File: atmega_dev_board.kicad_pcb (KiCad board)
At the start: 2 copper layers, 40 parts, among them J1 GPIO Header, J2 USB_B_Micro, J3 GPIO Header, J4 ICSP Header, Q1 Q_PMOS_DGS, SW1 SW_Push, U1 LM358, U2 NCV8114ASN330T1G, U3 NCV8114ASN330T1G, U4 ATmega328P-A, U5 CH340G, Y1 Crystal_GND23, Y2 Crystal_GND23

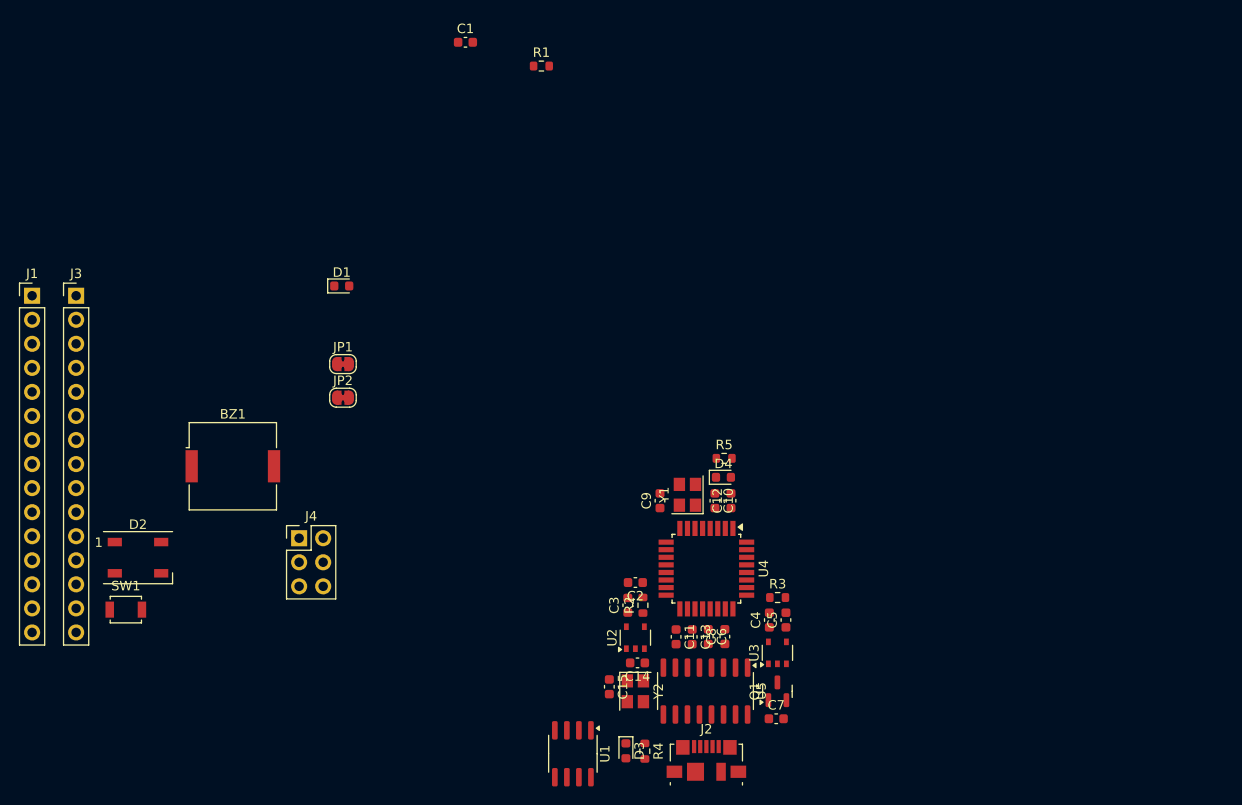
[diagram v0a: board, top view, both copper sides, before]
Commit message: Move to USB C and CP2102
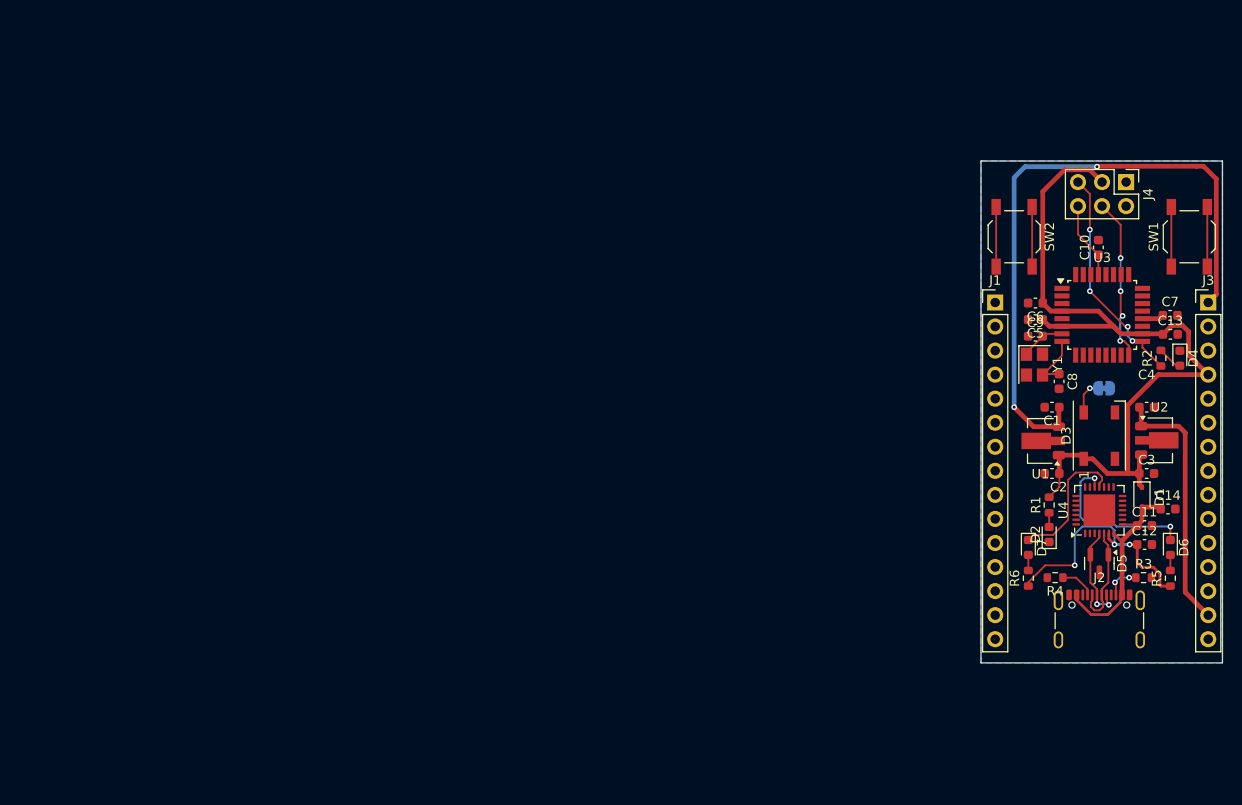
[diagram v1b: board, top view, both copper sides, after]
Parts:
- removed BZ1: Buzzer, Buzzer_Beeper:Buzzer_Murata_PKMCS0909E
- removed C15: 22p, Capacitor_SMD:C_0603_1608Metric
- removed JP2: Solder Jumper NC, Jumper:SolderJumper-2_P1.3mm_Bridged_RoundedPad1.0x1.5mm
- removed Q1: Q_PMOS_DGS, Package_TO_SOT_SMD:SOT-23
- removed U5: CH340G, Package_SO:SOIC-16_3.9x9.9mm_P1.27mm
- removed Y2: Crystal_GND23, Crystal:Crystal_SMD_3225-4Pin_3.2x2.5mm
- added D5: SM712_SOT23, Package_TO_SOT_SMD:SOT-23, F.Cu at (228.5, 117.0)
- added D6: LED, LED_SMD:LED_0603_1608Metric, F.Cu at (236.0, 115.3)
- added D7: LED, LED_SMD:LED_0603_1608Metric, F.Cu at (221.0, 115.3)
- added R6: 1k, Resistor_SMD:R_0603_1608Metric, F.Cu at (221.0, 118.6)
- added SW2: Push button switch, Button_Switch_SMD:SW_SPST_TL3342, F.Cu at (219.5, 82.5)
- C10: value 22p -> 100n
- C11, C2, C4, C5: value 10u -> 100n
- C14: value 22p -> 10u
- C8: value 100n -> 22p
- D1: value D_Small -> Diode Schottky; footprint Diode_SMD:D_0603_1608Metric -> Diode_SMD:D_SOD-323
- D2: value WS2812B -> LED; footprint LED_SMD:LED_WS2812B_PLCC4_5.0x5.0mm_P3.2mm -> LED_SMD:LED_0603_1608Metric
- D3: value LED_Small -> WS2812B; footprint LED_SMD:LED_0603_1608Metric -> LED_SMD:LED_WS2812B_PLCC4_5.0x5.0mm_P3.2mm
- D4: value LED_Small -> LED
- J1, J3: value GPIO Header -> 1x15 Pin Header
- J2: value USB_B_Micro -> USB_C_Receptacle_USB2.0_16P; footprint Connector_USB:USB_Micro-B_Molex_47346-0001 -> Connector_USB:USB_C_Receptacle_GCT_USB4105-xx-A_16P_TopMnt_Horizontal
- JP1: value Solder Jumper NC -> Closed Solder Jumper; moved to B.Cu
- R1: value 100 -> 1k
- R3, R4: value 1k -> 5k1
- SW1: value SW_Push -> Push button switch; footprint Button_Switch_SMD:SW_SPST_B3U-1000P -> Button_Switch_SMD:SW_SPST_TL3342
- U1: value LM358 -> L78L05_SOT89; footprint Package_SO:SOIC-8_3.9x4.9mm_P1.27mm -> Package_TO_SOT_SMD:SOT-89-3
- U2: value NCV8114ASN330T1G -> L78L33_SOT89; footprint Package_SO:TSOP-5_1.65x3.05mm_P0.95mm -> Package_TO_SOT_SMD:SOT-89-3
- U3: value NCV8114ASN330T1G -> ATmega328P-A; footprint Package_SO:TSOP-5_1.65x3.05mm_P0.95mm -> Package_QFP:TQFP-32_7x7mm_P0.8mm
- U4: value ATmega328P-A -> CP2102N-Axx-xQFN28; footprint Package_QFP:TQFP-32_7x7mm_P0.8mm -> Package_DFN_QFN:QFN-28-1EP_5x5mm_P0.5mm_EP3.35x3.35mm
- Y1: value Crystal_GND23 -> Crystal 16MHz
- moved J3 119.6 mm to (240.0, 89.4)
- moved SW1 119.0 mm to (238.0, 82.5), turned to 90 degrees
- moved J1 101.7 mm to (217.5, 89.4)
- moved D2 96.3 mm to (223.2, 113.9), turned to 90 degrees
- moved J4 95.1 mm to (231.3, 76.7), turned to -90 degrees
- moved D1 87.4 mm to (233.0, 110.0), turned to -90 degrees
- moved JP1 80.4 mm to (229.0, 98.5), turned to 180 degrees
- moved C1 73.0 mm to (223.5, 100.5), turned to 180 degrees
- moved R1 70.9 mm to (223.2, 110.8), turned to -90 degrees
- moved R2 60.6 mm to (235.0, 95.3)
- moved D3 60.1 mm to (228.5, 103.5), turned to 90 degrees
- moved C13 59.8 mm to (236.0, 92.8), turned to 0 degrees
- moved C7 59.5 mm to (236.0, 90.8)
- moved U1 59.4 mm to (222.3, 104.1), turned to 180 degrees
- moved U2 59.2 mm to (234.9, 104.0), turned to 0 degrees
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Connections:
- C1 pad 1: +5V -> +VDC
- C10 pad 1: GND -> /RESET
- C10 pad 2: Net-(U4-XTAL1/PB6) -> GND
- C11 pad 1: +5V -> VBUS
- C12 pad 1: +5V -> /CP_VDD
- C14 pad 1: /CH_XI -> VBUS
- C3 pad 1: +VDC -> +5V
- C4 pad 1: +5V -> +3V3
- C5 pad 1: +3V3 -> +5V
- C6 pad 1: /AREF -> +5V
- C7 pad 1: VBUS -> /AREF
- C8 pad 1: /CH_3V -> /AT_XTAL2
- C9 pad 1: Net-(U4-XTAL2/PB7) -> GND
- C9 pad 2: GND -> /AT_XTAL1
- D1 pad 1: /BZ+ -> +5V
- D1 pad 2: GND -> VBUS
- D2 pad 1: +5V -> GND
- D2 pad 2: unconnected-(D2-DOUT-Pad2) -> /LED_PWR
- D3 pad 1: GND -> +5V
- D3 pad 2: /LED_PWR -> unconnected-(D3-DOUT-Pad2)
- JP1 pad 1: /D9 -> /D11
- JP1 pad 2: /BZ+ -> /RGB_DIN
- R1 pad 1: /RGB_R -> +5V
- R1 pad 2: /RGB_DIN -> /LED_PWR
- R2 pad 1: +VDC -> /D13
- R2 pad 2: Net-(U2-EN) -> /LED_USR
- R3 pad 1: +5V -> /USB_CC2
- R3 pad 2: Net-(U3-EN) -> GND
- R4 pad 1: +5V -> /USB_CC1
- R4 pad 2: /LED_PWR -> GND
- R5 pad 1: /D13 -> /CP_VDD
- R5 pad 2: /LED_USR -> /LED_TXT
- SW1 pad 1: /RESET -> /D9
- U1 pad 1: Net-(Q1-G) -> +5V
- U1 pad 2: +3V3 -> GND
- U2 pad 1: +VDC -> +3V3
- U2 pad 3: Net-(U2-EN) -> +5V
- U3 pad 1: +5V -> /D3
- U3 pad 2: GND -> /D4
- U3 pad 3: Net-(U3-EN) -> GND
- U3 pad 4: unconnected-(U3-NC-Pad4) -> +5V
- U3 pad 5: +3V3 -> GND
- U4 pad 1: /D3 -> unconnected-(U4-~{DCD}-Pad1)
- U4 pad 10: /D6 -> unconnected-(U4-NC-Pad10)
- U4 pad 11: /D7 -> unconnected-(U4-~{SUSPEND}-Pad11)
- U4 pad 12: /D8 -> unconnected-(U4-SUSPEND-Pad12)
- U4 pad 13: /D9 -> unconnected-(U4-CHREN-Pad13)
- U4 pad 14: /D10 -> unconnected-(U4-CHR1-Pad14)
- U4 pad 15: /D11 -> unconnected-(U4-CHR0-Pad15)
- U4 pad 16: /D12 -> unconnected-(U4-~{WAKEUP}/GPIO.3-Pad16)
- U4 pad 17: /D13 -> unconnected-(U4-RS485/GPIO.2-Pad17)
- U4 pad 18: +5V -> /RXT
- U4 pad 19: /A6 -> /TXT
- U4 pad 2: /D4 -> unconnected-(U4-~{RI}/CLK-Pad2)
- U4 pad 20: /AREF -> unconnected-(U4-GPIO.6-Pad20)
- U4 pad 21: GND -> unconnected-(U4-GPIO.5-Pad21)
- U4 pad 22: /A7 -> unconnected-(U4-GPIO.4-Pad22)
- U4 pad 23: /A0 -> unconnected-(U4-~{CTS}-Pad23)
- U4 pad 24: /A1 -> unconnected-(U4-~{RTS}-Pad24)
- U4 pad 25: /A2 -> /D0
- U4 pad 26: /A3 -> /D1
- U4 pad 27: /A4 -> unconnected-(U4-~{DSR}-Pad27)
- U4 pad 28: /A5 -> /RESET
- U4 pad 29: /RESET -> GND
- U4 pad 4: +5V -> /USB_D+
- U4 pad 5: GND -> /USB_D-
- U4 pad 6: +5V -> /CP_VDD
- U4 pad 7: Net-(U4-XTAL1/PB6) -> VBUS
- U4 pad 8: Net-(U4-XTAL2/PB7) -> VBUS
- U4 pad 9: /D5 -> unconnected-(U4-~{RST}-Pad9)
- Y1 pad 1: Net-(U4-XTAL1/PB6) -> /AT_XTAL1
- Y1 pad 3: GND -> /AT_XTAL2
- Y1 pad 4: Net-(U4-XTAL2/PB7) -> GND
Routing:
- net +5V: track 0.00 -> 85.8 mm
- net +VDC: track 0.00 -> 67.7 mm, vias 0 -> 2
- net +3V3: track 0.00 -> 27.3 mm
- net /CP_VDD: track 0.00 -> 26.5 mm, vias 0 -> 3
- net /D13: track 0.00 -> 23.8 mm, vias 0 -> 4
- net VBUS: track 0.00 -> 23.5 mm
- net /TXT: track 0.00 -> 17.6 mm, vias 0 -> 2
- net /D12: track 0.00 -> 17.3 mm, vias 0 -> 4
- net /RXT: track 0.00 -> 14.6 mm
- net /RESET: track 0.00 -> 14.4 mm
- net GND: track 0.00 -> 12.6 mm
- net /USB_D-: track 0.00 -> 11.2 mm
- net /USB_D+: track 0.00 -> 10.6 mm, vias 0 -> 2
- net /D9: track 0.00 -> 6.30 mm
- net /AT_XTAL2: track 0.00 -> 6.19 mm
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- added copper zone on B.Cu, net GND
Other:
- board outline added: 25.5 x 53 mm

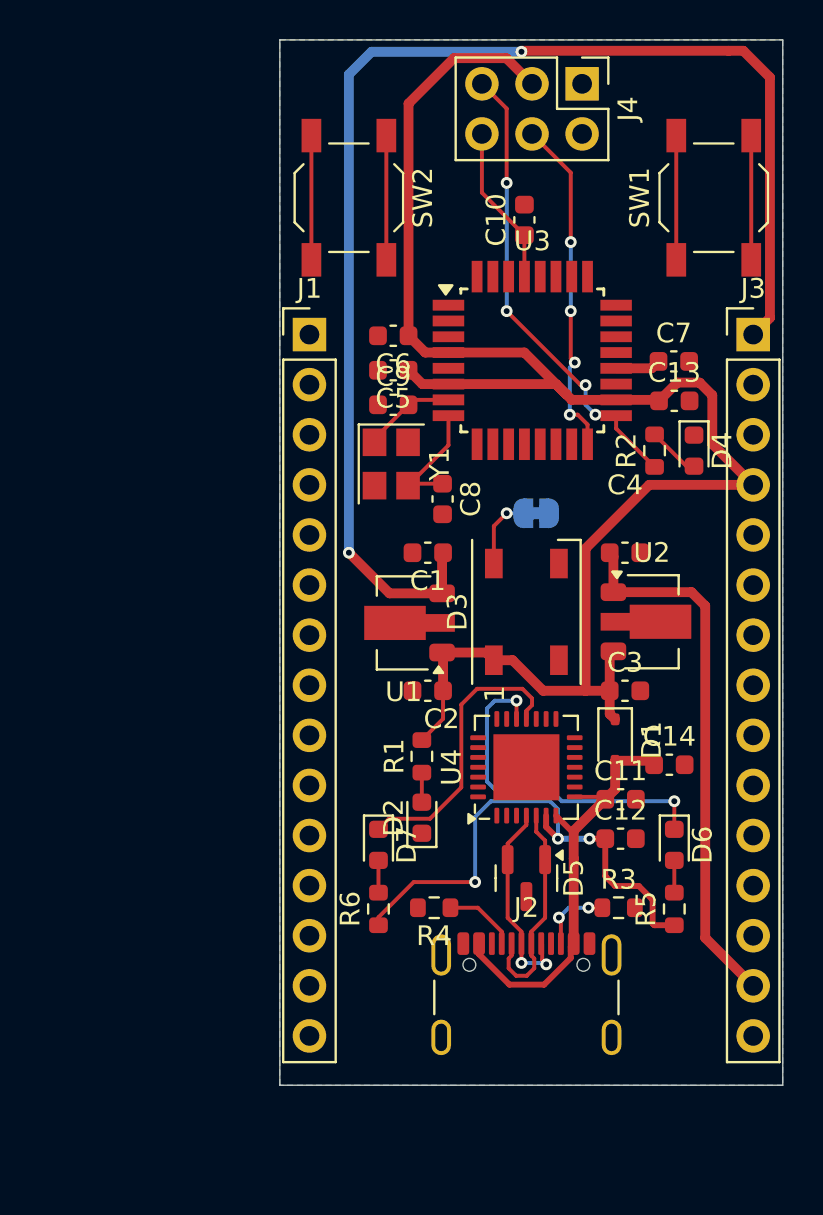
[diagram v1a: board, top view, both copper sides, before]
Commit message: Adjust pin header and board size to match 0m1" pitch
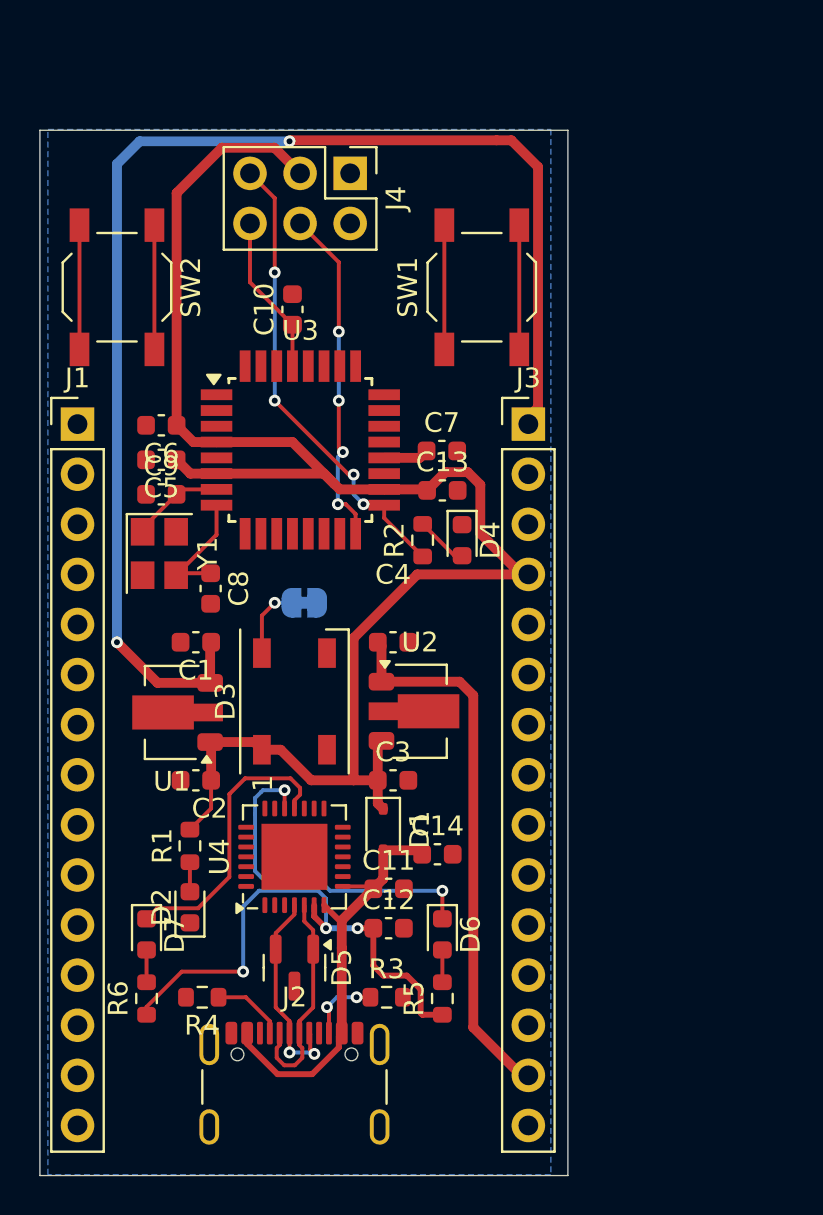
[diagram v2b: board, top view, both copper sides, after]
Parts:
- moved C10 12.6 mm to (216.6, 88.2)
- moved C11 12.6 mm to (221.5, 117.5)
- moved C12 12.6 mm to (221.5, 119.5)
- moved R3 12.6 mm to (221.4, 123.0)
- moved U2 12.6 mm to (223.1, 108.5)
- moved U3 12.6 mm to (217.0, 95.3)
- moved Y1 12.6 mm to (209.9, 100.5)
- moved U1 12.6 mm to (210.5, 108.6)
- moved C1 12.6 mm to (211.7, 105.0)
- moved C13 12.6 mm to (224.2, 97.3)
- moved C14 12.6 mm to (224.0, 115.8)
- moved C2 12.6 mm to (211.7, 112.0)
- moved C3 12.6 mm to (221.7, 112.0)
- moved C4 12.6 mm to (221.7, 105.0)
- moved C5 12.6 mm to (210.0, 95.8)
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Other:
- board size 25.5 x 53 mm -> 26.8 x 53 mm

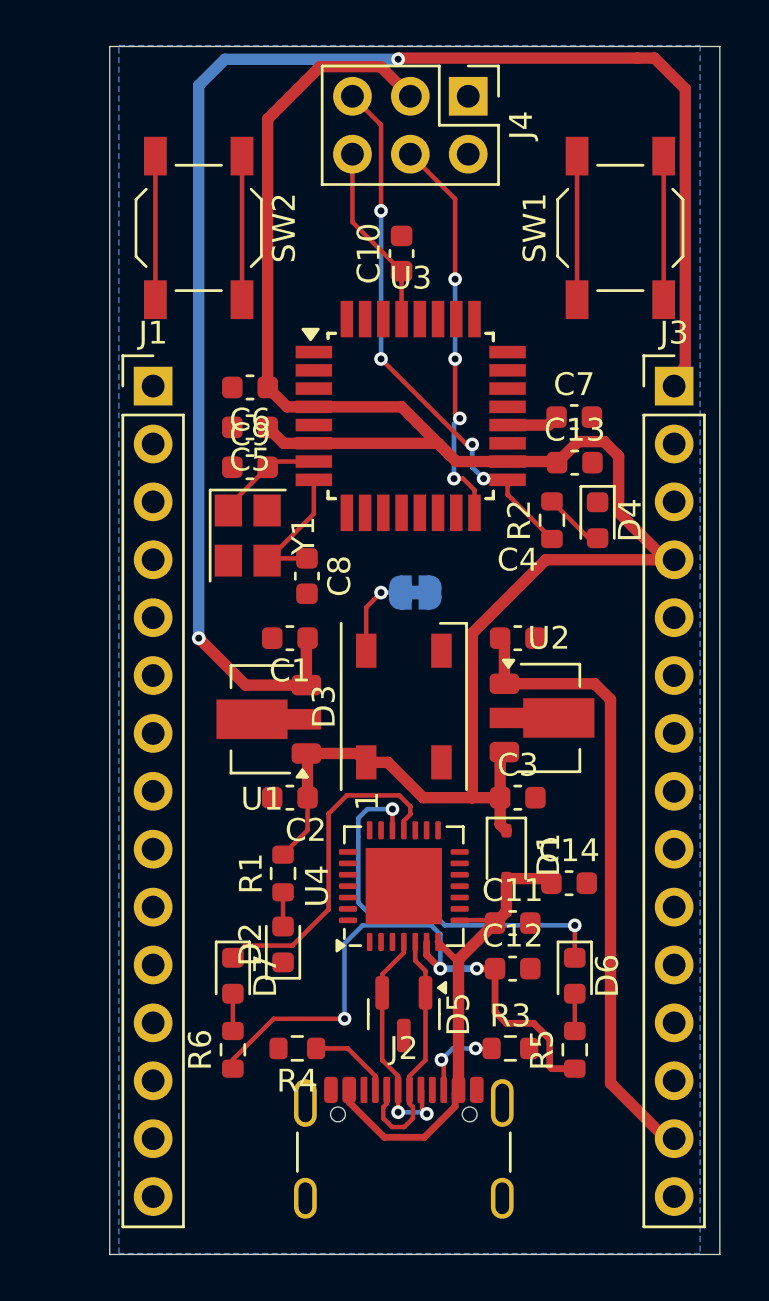
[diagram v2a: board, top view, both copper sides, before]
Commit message: New placements of PCB
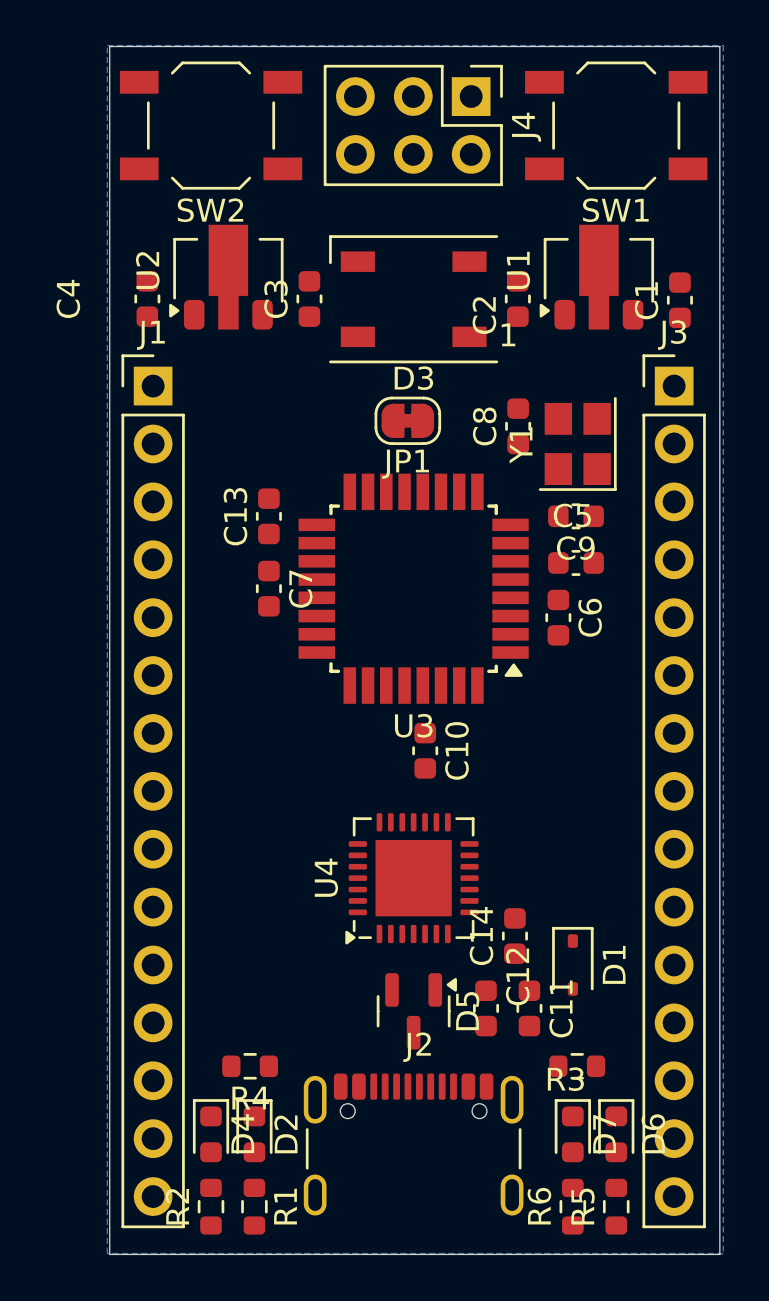
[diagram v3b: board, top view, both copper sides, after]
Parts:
- JP1: moved to F.Cu
- moved R2 33.6 mm to (208.3, 130.0)
- moved D4 31.8 mm to (208.3, 126.8)
- moved U1 24.6 mm to (225.3, 88.9), turned to 90 degrees
- moved U2 24.2 mm to (209.0, 88.9), turned to 90 degrees
- moved C2 24.1 mm to (221.7, 90.2), turned to 90 degrees
- moved C3 23.7 mm to (212.6, 90.2), turned to 90 degrees
- moved C1 22.6 mm to (228.9, 90.2), turned to 90 degrees
- moved C4 22.0 mm to (205.5, 90.2), turned to 90 degrees
- moved C10 21.8 mm to (217.7, 110.0), turned to -90 degrees
- moved D3 17.9 mm to (217.2, 90.2), turned to 180 degrees
- moved C6 16.9 mm to (223.5, 104.1), turned to -90 degrees
- moved D7 16.5 mm to (224.2, 126.8)
- moved R6 16.4 mm to (224.2, 130.0)
- moved C5 15.5 mm to (224.3, 101.7), turned to 0 degrees
- moved C7 15.4 mm to (210.8, 102.9), turned to -90 degrees
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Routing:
- net +5V: track 85.8 -> 0.00 mm
- net +VDC: track 67.7 -> 0.00 mm, vias 2 -> 0
- net +3V3: track 27.3 -> 0.00 mm
- net /CP_VDD: track 26.5 -> 0.00 mm, vias 3 -> 0
- net /D13: track 23.8 -> 0.00 mm, vias 4 -> 0
- net VBUS: track 23.5 -> 0.00 mm
- net /TXT: track 17.6 -> 0.00 mm, vias 2 -> 0
- net /D12: track 17.3 -> 0.00 mm, vias 4 -> 0
- net /RXT: track 14.6 -> 0.00 mm
- net /RESET: track 14.4 -> 0.00 mm
- net GND: track 12.6 -> 0.00 mm
- net /USB_D-: track 11.2 -> 0.00 mm
- net /USB_D+: track 10.6 -> 0.00 mm, vias 2 -> 0
- net /D9: track 6.30 -> 0.00 mm
- net /AT_XTAL2: track 6.19 -> 0.00 mm
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- added copper zone on In1.Cu, net GND
- added copper zone on In2.Cu, net GND
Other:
- copper layers 2 -> 4
